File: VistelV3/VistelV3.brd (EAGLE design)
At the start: 120 x 120 mm, 181 parts, among them IC1 LD117ADT33TR, IC5 SI7006-A10-IM, J2 RJ45-ABRACON-11108B, J3 RJ45-ABRACON-11108B, K1 ZF112, K2 ZF112, K3 ZF112, K4 ZF112, T1 MOSFET-NCHANNELBSS123LT1G, T2 MOSFET-NCHANNELBSS123LT1G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

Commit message: Update2
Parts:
- moved C51 118.9 mm to (64.8, 3.30)
- moved R3 92.3 mm to (50.8, 11.1), turned to 270 degrees
- moved C30 30.0 mm to (95.8, 15.0)
- moved LED13 11.5 mm to (52.6, 20.6)
- moved R2 10.5 mm to (50.7, 7.40), turned to 270 degrees
- moved C3 7.69 mm to (54.1, 4.54), turned to 180 degrees
- moved IC1 5.92 mm to (65.0, 11.6)
- moved R44 5.11 mm to (66.8, 22.4)
- moved C4 4.79 mm to (58.9, 4.33)
- moved L1 4.34 mm to (57.0, 3.41)
- moved U$18 0.32 mm to (54.2, 7.76), turned to 90 degrees
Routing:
- net +12V: track 8.27 -> 36.1 mm, vias 0 -> 2
- net GND: track 44.0 -> 71.8 mm
- net +5V: track 0.00 -> 11.9 mm
- net N$6: track 0.00 -> 7.48 mm, vias 0 -> 3
- net N$20: track 0.00 -> 4.00 mm
- net N$19: track 0.00 -> 2.33 mm

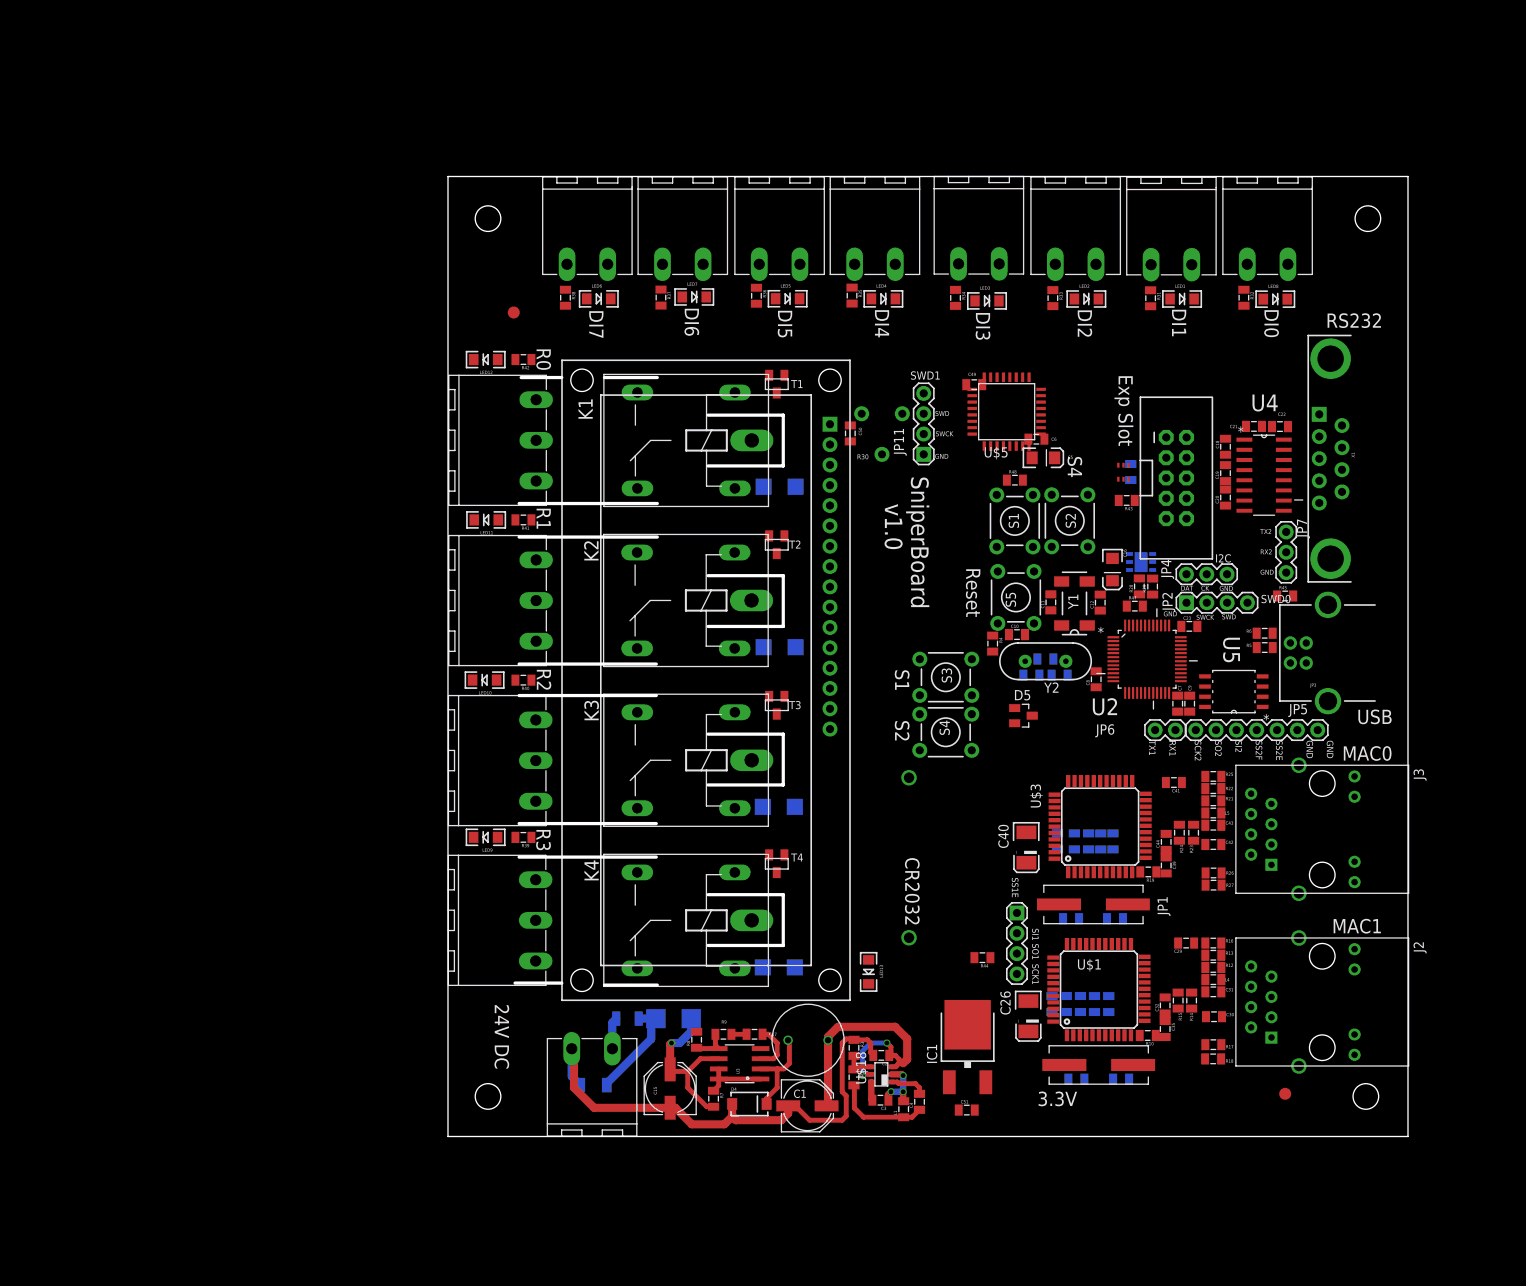
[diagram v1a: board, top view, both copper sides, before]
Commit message: Updated Power suply section
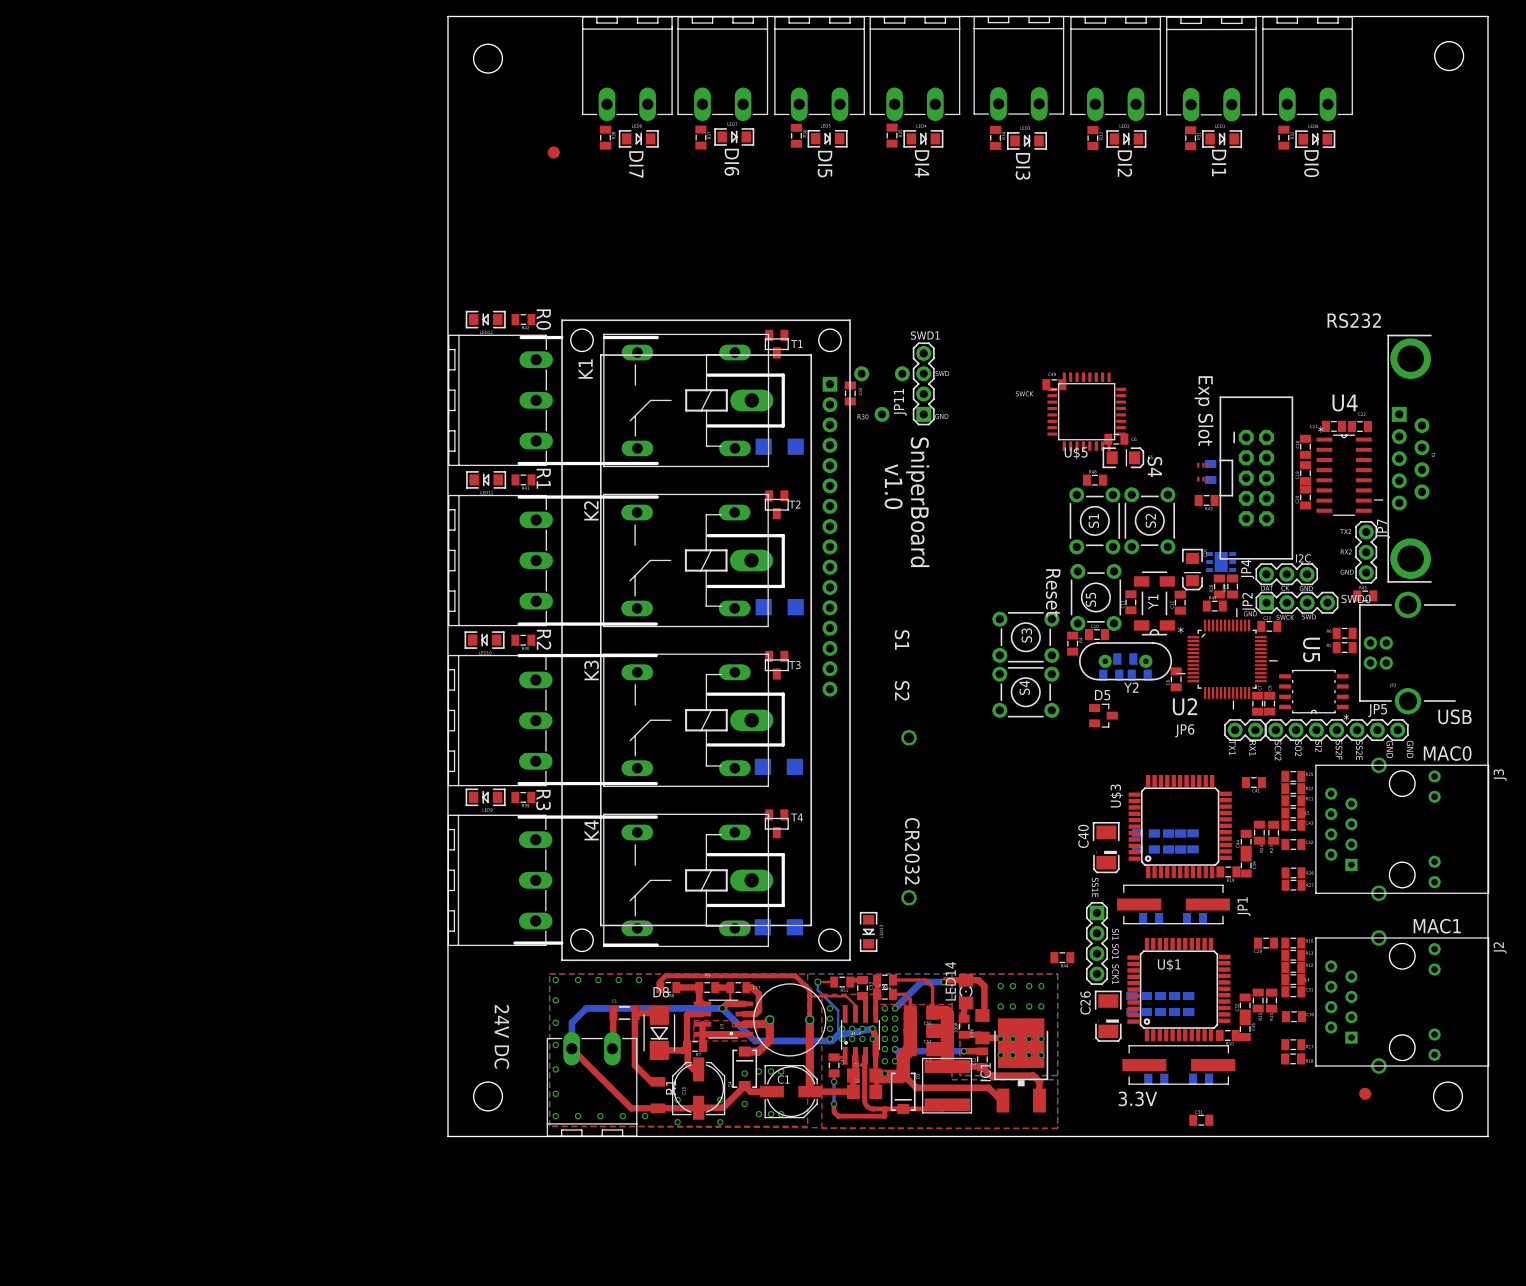
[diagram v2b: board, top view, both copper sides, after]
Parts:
- removed R2: 41.2K, SparkFun-Passives:0805
- removed R3: 10K, SparkFun-Passives:0805
- added 330R, R50: 10K, SparkFun-Passives:0805
- added C52: 0.1uF, SparkFun-Passives:0805
- added C53: 1.5nF, SparkFun-Passives:0805
- added C54, C55, C56, C57: 10uF CC1206ZKY5V7BB106, SparkFun-Passives:1206
- added D1: (no value), SparkFun-DiscreteSemi:SMA-DIODE
- added LED14: (no value), SparkFun-LED:FKIT-LED-1206
- added R49: 15.5K, SparkFun-Passives:0805
- added R51: 12K, SparkFun-Passives:0805
- C2, C3: value 0.1uF -> 10uF CC1206ZKY5V7BB106; device SparkFun-Passives:0805 -> SparkFun-Passives:1206
- C4: value 22uF 6.3V -> 10nF
- L1: value 4.7uH JMK212BJ476MG -> 22uH NR6045T220M; device SparkFun-Passives:0805 -> SparkFun-Passives:NR6045-IND
- U$18: value (none) -> ACT4060A; device VistelV3:TSOT23-6_DDC -> VistelV3:SO08
- moved C51 29.3 mm to (94.2, 2.03)
- moved U$10 20.6 mm to (22.4, 129.0)
- moved U$11 20.6 mm to (34.4, 129.0)
- moved U$12 20.6 mm to (58.4, 129.0)
- moved U$13 20.6 mm to (83.5, 129.0)
- moved U$6 20.6 mm to (107.5, 129.0)
- moved U$9 20.6 mm to (46.5, 129.0)
- moved FID2 20.6 mm to (13.2, 123.0)
- moved LED1 20.6 mm to (96.8, 124.7)
- moved LED2 20.6 mm to (84.8, 124.7)
- moved LED3 20.6 mm to (72.4, 124.4)
- moved LED4 20.6 mm to (59.4, 124.7)
- moved LED5 20.6 mm to (47.5, 124.7)
- moved LED6 20.6 mm to (23.8, 124.7)
- moved LED7 20.6 mm to (35.8, 124.9)
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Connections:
- new net N$18: C4.2, D1.C, L1.P$1, U$18.3
- new net N$23: C53.2, U$18.6
- new net N$32: C53.1, R51.1
- net +12V: now also C54.1, U$18.2, U$18.7; no longer U$18.3, U$18.5
- net +5V: now also C3.1, C52.1, C55.1, C57.1, IC1.3, L1.P$2, R49.1; no longer C4.1, L1.1, R2.2
- net 3.3V: now also 330R.1, C56.1
- net GND: now also C3.2, C52.2, C54.2, C55.2, C56.2, C57.2, D1.A, LED14.C, R50.2, R51.2, U$18.4; no longer C4.2, R3.1, U$18.1
- net N$19: now also R49.2, R50.1, U$18.5; no longer C3.2, U$18.6
- net N$20: now also 330R.2, LED14.A; no longer IC1.3, R2.1, R3.2, U$18.4
- net N$6: now also C4.1, U$18.1; no longer C3.1, L1.2, U$18.2
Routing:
- net GND: track 71.8 -> 155.3 mm, vias 0 -> 54
- net N$18: track 0.00 -> 28.9 mm, vias 0 -> 2
- net +5V: track 11.9 -> 35.5 mm
- net +12V: track 36.1 -> 50.5 mm, vias 2 -> 0
- net VIN: track 21.1 -> 13.4 mm, vias 1 -> 0
- net 3.3V: track 0.00 -> 7.57 mm, vias 0 -> 16
- net N$6: track 7.48 -> 1.48 mm, vias 3 -> 0
- net N$23: track 0.00 -> 2.38 mm
- net N$24: track 11.8 -> 9.67 mm
- net N$19: track 2.33 -> 4.30 mm
- net N$20: track 4.00 -> 2.07 mm
- net N$32: track 0.00 -> 1.64 mm
- net N$5: track 12.8 -> 13.5 mm
- net N$4: track 3.97 -> 4.57 mm
- net N$2: track 0.00 -> 0.51 mm
- added copper zone on layer 1, net 3.3V
- added copper zone on layer 16, net 3.3V
- added copper zone on layer 1, net GND
- added copper zone on layer 16, net GND
- added copper zone on layer 1, net VIN2
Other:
- board size 120 x 120 mm -> 130 x 140 mm
